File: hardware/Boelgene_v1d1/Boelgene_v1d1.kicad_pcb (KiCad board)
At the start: 2 copper layers, 86.4 x 53.8 mm, 70 parts, among them J1 batt, J2 pressure3, J3 pressure2, J4 pressure1, J5 pressure4, U1 Pico, U2 MCP3008, U3 PT8211-pt8211

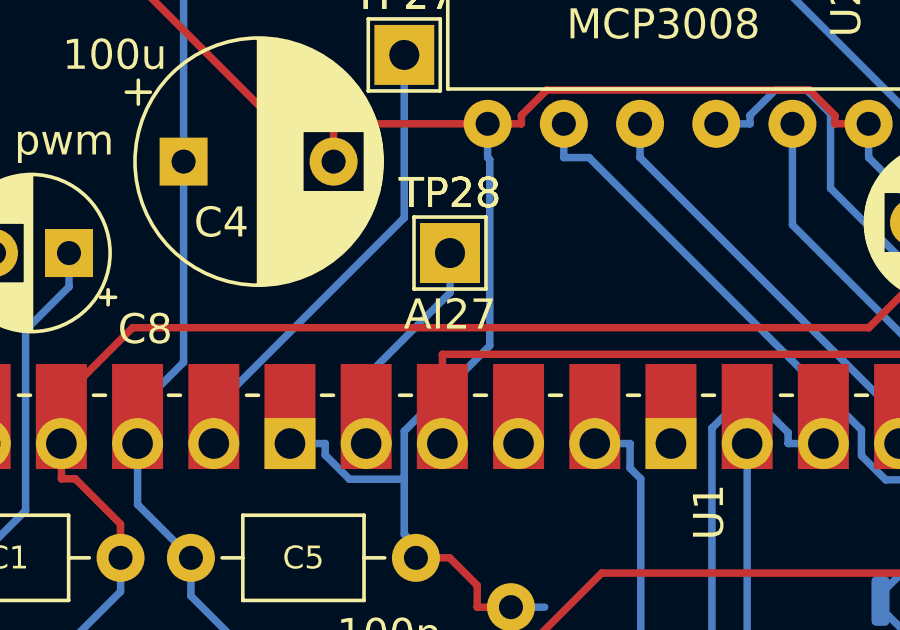
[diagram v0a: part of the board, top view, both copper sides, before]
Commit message: Added correct ribbon input reference
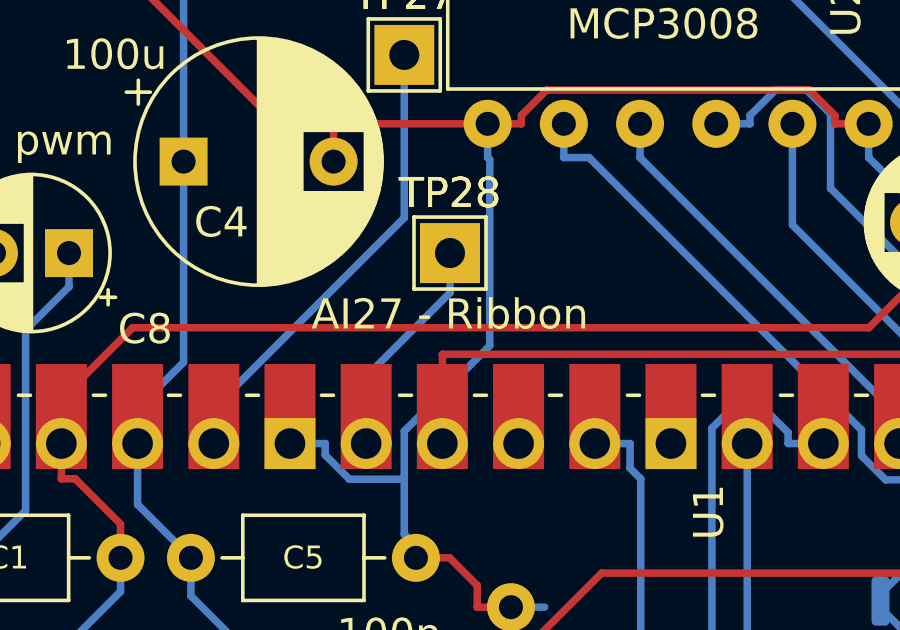
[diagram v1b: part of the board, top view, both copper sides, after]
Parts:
- TP28: value AI27 -> AI27 - Ribbon

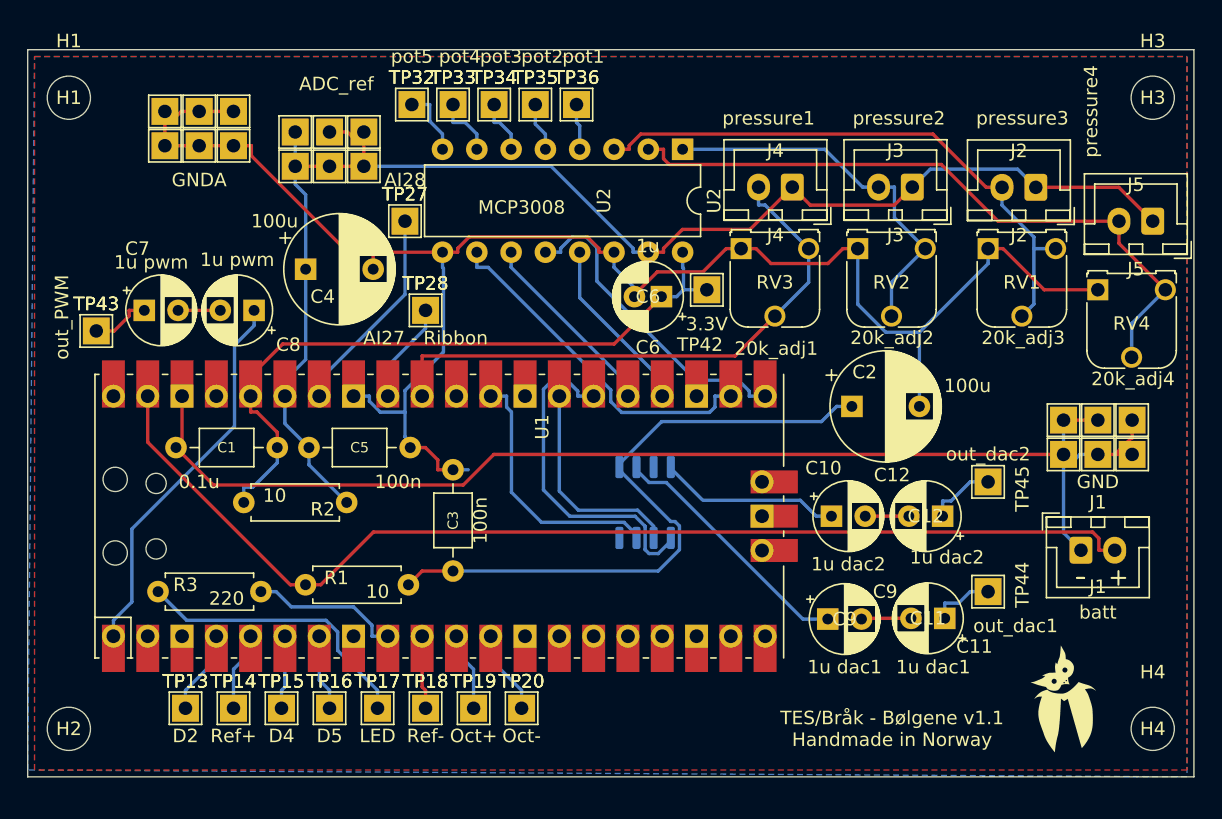
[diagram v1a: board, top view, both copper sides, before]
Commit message: Updated PCB with connectors
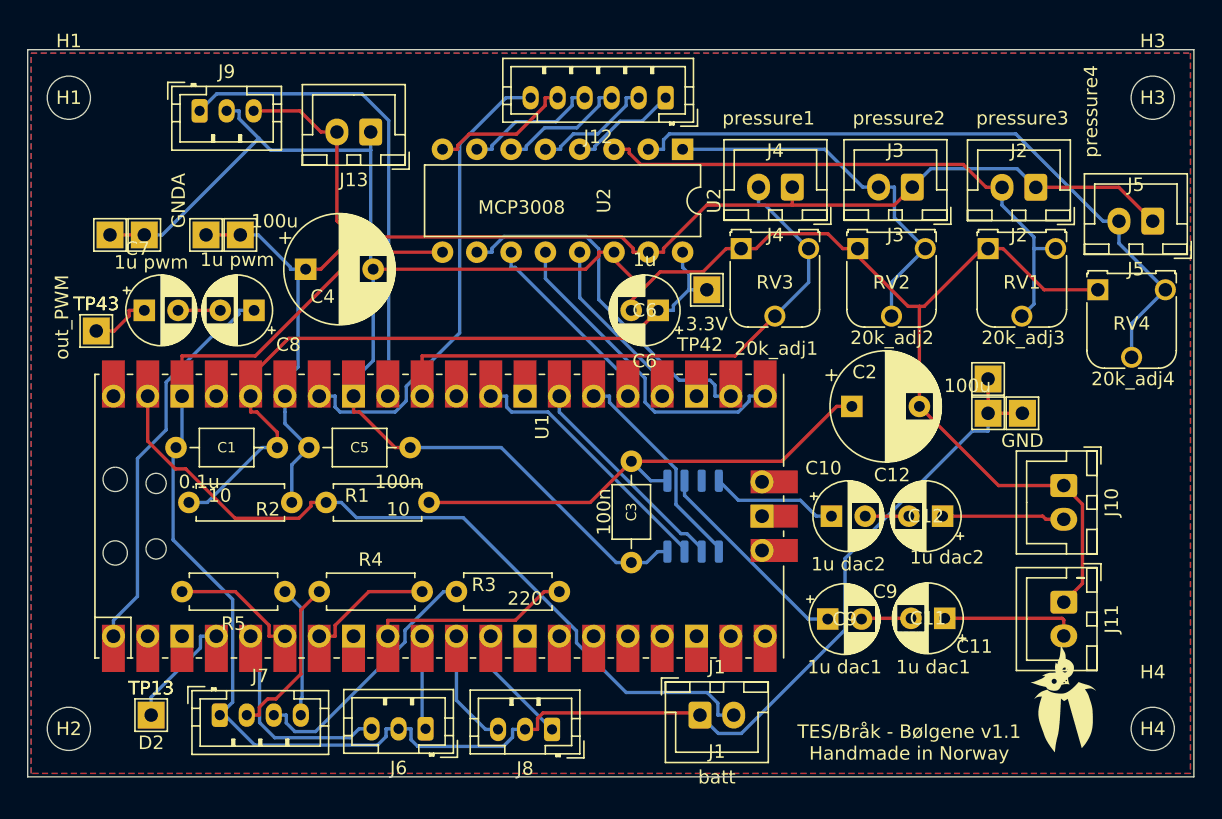
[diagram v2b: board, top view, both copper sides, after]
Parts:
- removed TP1, TP5, TP6: GND, TestPoint:TestPoint_THTPad_2.0x2.0mm_Drill1.0mm
- removed TP11, TP2, TP4, TP9: ADC_ref, TestPoint:TestPoint_THTPad_2.0x2.0mm_Drill1.0mm
- removed TP14: Ref+, TestPoint:TestPoint_THTPad_2.0x2.0mm_Drill1.0mm
- removed TP15: D4, TestPoint:TestPoint_THTPad_2.0x2.0mm_Drill1.0mm
- removed TP16: D5, TestPoint:TestPoint_THTPad_2.0x2.0mm_Drill1.0mm
- removed TP17: LED, TestPoint:TestPoint_THTPad_2.0x2.0mm_Drill1.0mm
- removed TP18: Ref-, TestPoint:TestPoint_THTPad_2.0x2.0mm_Drill1.0mm
- removed TP19: Oct+, TestPoint:TestPoint_THTPad_2.0x2.0mm_Drill1.0mm
- removed TP20: Oct-, TestPoint:TestPoint_THTPad_2.0x2.0mm_Drill1.0mm
- removed TP21, TP22, TP24, TP26: GNDA, TestPoint:TestPoint_THTPad_2.0x2.0mm_Drill1.0mm
- removed TP27: AI28, TestPoint:TestPoint_THTPad_2.0x2.0mm_Drill1.0mm
- removed TP28: AI27 - Ribbon, TestPoint:TestPoint_THTPad_2.0x2.0mm_Drill1.0mm
- removed TP32: pot5, TestPoint:TestPoint_THTPad_2.0x2.0mm_Drill1.0mm
- removed TP33: pot4, TestPoint:TestPoint_THTPad_2.0x2.0mm_Drill1.0mm
- removed TP34: pot3, TestPoint:TestPoint_THTPad_2.0x2.0mm_Drill1.0mm
- removed TP35: pot2, TestPoint:TestPoint_THTPad_2.0x2.0mm_Drill1.0mm
- removed TP36: pot1, TestPoint:TestPoint_THTPad_2.0x2.0mm_Drill1.0mm
- removed TP44: out_dac1, TestPoint:TestPoint_THTPad_2.0x2.0mm_Drill1.0mm
- removed TP45: out_dac2, TestPoint:TestPoint_THTPad_2.0x2.0mm_Drill1.0mm
- added J10: Right, Connector_JST:JST_XH_B2B-XH-A_1x02_P2.50mm_Vertical, F.Cu at (105.2, 110.0)
- added J11: Left (mono), Connector_JST:JST_XH_B2B-XH-A_1x02_P2.50mm_Vertical, F.Cu at (105.2, 118.6)
- added J12: pots, Connector_JST:JST_PH_B6B-PH-K_1x06_P2.00mm_Vertical, F.Cu at (75.7, 81.3)
- added J13: pots - power, Connector_JST:JST_XH_B2B-XH-A_1x02_P2.50mm_Vertical, F.Cu at (53.8, 83.8)
- added J6: R ref+ // Y ref-, Connector_JST:JST_PH_B3B-PH-K_1x03_P2.00mm_Vertical, F.Cu at (57.9, 128.0)
- added J7: LED // R- // W0 // Y+, Connector_JST:JST_PH_B4B-PH-K_1x04_P2.00mm_Vertical, F.Cu at (42.7, 127.0)
- added J8: Y oct- // R oct+, Connector_JST:JST_PH_B3B-PH-K_1x03_P2.00mm_Vertical, F.Cu at (67.3, 128.1)
- added J9: Ribbon, Connector_JST:JST_PH_B3B-PH-K_1x03_P2.00mm_Vertical, F.Cu at (41.2, 82.3)
- added R4: 220, Resistor_THT:R_Axial_DIN0207_L6.3mm_D2.5mm_P7.62mm_Horizontal, F.Cu at (50.0, 117.9)
- added R5: 220, Resistor_THT:R_Axial_DIN0207_L6.3mm_D2.5mm_P7.62mm_Horizontal, F.Cu at (47.5, 117.9)
- moved J1 30.7 mm to (78.2, 127.0)
- moved R3 22.1 mm to (60.2, 117.9)
- moved C3 15.5 mm to (73.2, 108.2), turned to -90 degrees
- moved TP10 10.5 mm to (41.7, 91.4), turned to -90 degrees
- moved TP3 10.1 mm to (44.2, 91.4), turned to -90 degrees
- moved TP23 10.0 mm to (34.5, 91.4), turned to 90 degrees
- moved TP25 6.78 mm to (37.1, 91.4), turned to 90 degrees
- moved TP12 6.37 mm to (99.6, 102.1)
- moved TP7 6.37 mm to (99.6, 104.6)
- moved TP8 6.37 mm to (102.1, 104.6)
- moved R1 6.28 mm to (58.2, 111.3)
- moved R2 4.06 mm to (48.0, 111.3)
- moved U3 3.70 mm to (77.7, 112.3)
- moved TP13 2.59 mm to (37.6, 127.0)
- moved C6 1.04 mm to (75.1, 97.0)
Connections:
- U1 pad 34: Net-(TP27-Pad1) -> /analog_input_28
- U2 pad 9: GNDA -> GND
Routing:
- net GNDA: track 128.8 -> 171.6 mm
- net GND: track 93.6 -> 132.4 mm
- net /analog_input_28: track 0.00 -> 35.1 mm
- net Net-(U1-Pad32): track 7.51 -> 35.8 mm
- net batt+: track 82.1 -> 57.3 mm
- net Net-(TP27-Pad1): track 15.6 -> 0.00 mm
- net Net-(J7-Pad2): track 0.00 -> 12.3 mm
- net filtered_vcc: track 48.5 -> 37.5 mm
- net Net-(U1-Pad5): track 5.86 -> 15.7 mm
- net Net-(J7-Pad4): track 0.00 -> 9.71 mm
- net Net-(U1-Pad26): track 25.2 -> 16.0 mm
- net Net-(U2-Pad8): track 5.03 -> 10.6 mm
- net Net-(U2-Pad7): track 4.57 -> 10.1 mm
- net Net-(U2-Pad6): track 4.06 -> 9.50 mm
- net Net-(C11-Pad1): track 4.69 -> 10.0 mm
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
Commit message: Updated PCB
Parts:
- J11: value Left (mono) -> LEFT (mono)
- U1: footprint Pico:RPi_Pico_SMD_TH -> Pico:RPi_Pico_TH
- moved G*** 1.44 mm to (106.2, 127.0)
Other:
- board text added: "3.3/analog"
- board text added: "LEDs Y+/R-/W0"
- board text added: "LEFT mono"
- board text added: "Oct Y-//R+"
- board text added: "Pots <-"
- board text added: "RIGHT"
- board text added: "Ref Y-//R+"
- board text added: "Ribbon (prec pot 10k)"
- board text added: "pots' power"

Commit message: Updated pcb
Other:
- board text added: "I2S: BCK: GI20 WS: GP21 DIN: GP22 ADC: SPI0 CLK: GP18 RX: GP16 TX: GP19 CS: GP17 RIBBON: GP27"
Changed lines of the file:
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@@
   (gr_line (start 106.68 116.84) (end 106.172 116.84) (layer "F.SilkS") (width 0.15))
   (gr_rect (start 28.448 77.724) (end 114.808 131.572) (layer "Edge.Cuts") (width 0.1) (fill none))
+  (gr_text "I2S:\nBCK: GI20\nWS: GP21\nDIN: GP22\n\nADC: SPI0\nCLK: GP18\nRX: GP16\nTX: GP19\nCS: GP17\n\nRIBBON: GP27\n" (at 114.427 110.998) (layer "B.SilkS")
+    (effects (font (size 0.8 0.8) (thickness 0.1)) (justify left mirror))
+  )
   (gr_text "Oct\nY-//R+" (at 70.866 127 90) (layer "F.SilkS")
     (effects (font (size 0.8 0.8) (thickness 0.1)))

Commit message: Added brak logo
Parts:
- added G***: LOGO, brak:brak_logo, B.Cu at (81.7, 86.4)
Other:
- board text added: "TES"

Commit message: Added Mozzi ref
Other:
- board text added: "Powered by Mozzi"
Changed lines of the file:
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@@
     (effects (font (size 0.8 0.8) (thickness 0.1)) (justify left mirror))
+  )
+  (gr_text "Powered by Mozzi" (at 90.805 128.905) (layer "B.SilkS")
+    (effects (font (size 2 2) (thickness 0.3)) (justify mirror))
   )
   (gr_text "TES" (at 69.342 125.603) (layer "B.SilkS")
